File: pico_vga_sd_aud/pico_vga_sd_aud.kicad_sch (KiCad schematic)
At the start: 71 parts, among them J1 AudioJack3, J2 AudioJack3, J3 Micro_SD_Card, J4 L77HDE15SD1CH4F, J5 USB_B_Micro, J6 Conn_01x02, J7 Conn_02x03_Odd_Even, SW1 SW_Push, SW2 SW_Push, SW3 SW_Push, SW4 SW_Push, U1 TLV70033_SOT23-5, U2 Pico, U3 NC7WZ16P6X, U4 PCM5101A

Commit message: pico: Update footprint to new one with a keepout
Update symbol to new one
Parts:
- U2: footprint RPi_Pico:RPi_Pico_SMD_TH -> RaspberryPi_Pico_SMD:RPi_Pico_SMD; symbol RPi_Pico:Pico -> MCU_RaspberryPi_Pico:Pico

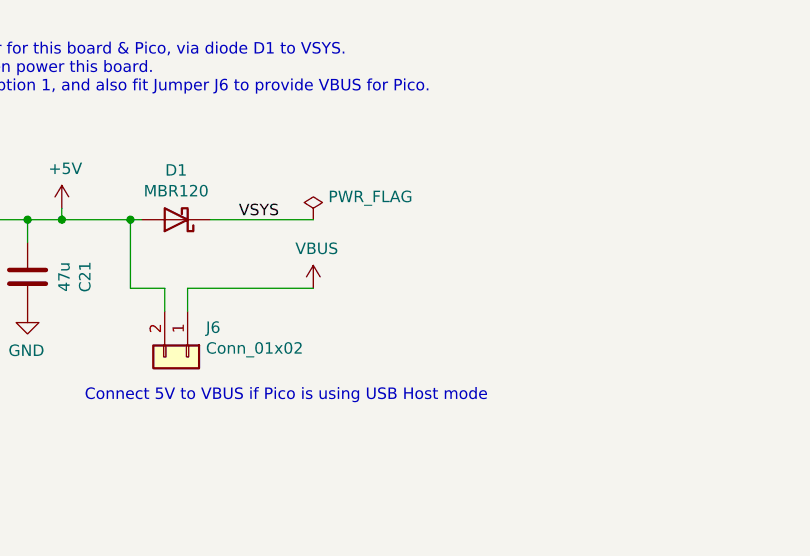
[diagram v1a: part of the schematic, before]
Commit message: pico: Get ERC to pass
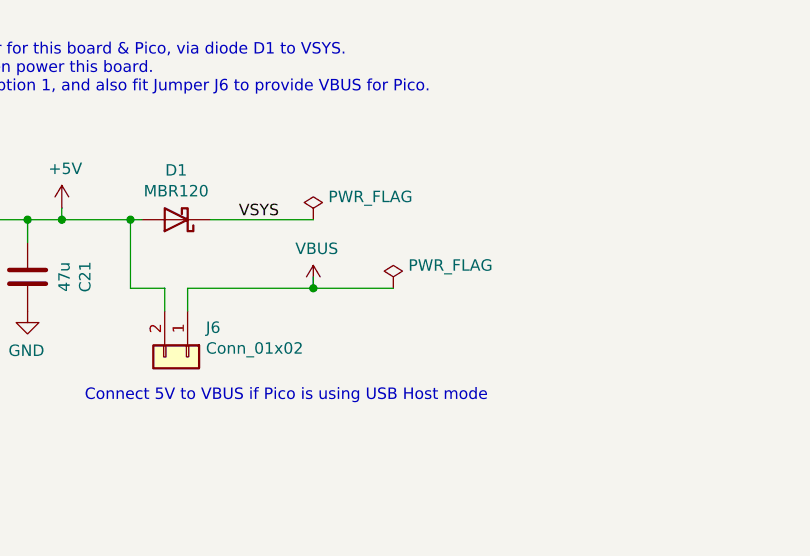
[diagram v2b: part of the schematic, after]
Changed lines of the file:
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@@
   (junction (at 317.5 120.65) (diameter 0) (color 0 0 0 0)
   )
+  (junction (at 109.22 45.72) (diameter 0) (color 0 0 0 0)
+  )
   (junction (at 148.59 254) (diameter 0) (color 0 0 0 0)
   )
@@
     (stroke (width 0) (type default))
   )
+  (wire (pts (xy 109.22 44.45) (xy 109.22 45.72))
+    (stroke (width 0) (type default))
+  )
   (wire (pts (xy 154.94 265.43) (xy 161.29 265.43))
     (stroke (width 0) (type default))
@@
     (stroke (width 0) (type default))
   )
+  (wire (pts (xy 109.22 45.72) (xy 118.11 45.72))
+    (stroke (width 0) (type default))
+  )
   (wire (pts (xy 91.44 130.81) (xy 107.95 130.81))
     (stroke (width 0) (type default))
@@
         )
       )
+    )
+  )
+  (symbol (lib_id "power:PWR_FLAG") (at 118.11 45.72 0) (unit 1)
+    (in_bom yes) (on_board yes) (dnp no)
+    (property "Reference" "#FLG01" (at 118.11 43.815 0)
+      (effects (font (size 1.27 1.27)) hide)
+    )
+    (property "Value" "PWR_FLAG" (at 124.46 43.18 0)
+      (effects (font (size 1.27 1.27)))
+    )
+    (property "Footprint" "" (at 118.11 45.72 0)
+      (effects (font (size 1.27 1.27)) hide)
+    )
+    (property "Datasheet" "~" (at 118.11 45.72 0)
+      (effects (font (size 1.27 1.27)) hide)
+    )
+    (pin "1")
+    (instances
+      (project "pico_vga_sd_aud"
+        (path "/d375fc5e-917b-4e0f-9a68-932a1e68a6b5"
+          (reference "#FLG01") (unit 1)
+        )
+      )
